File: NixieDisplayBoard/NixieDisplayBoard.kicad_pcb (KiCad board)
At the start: 2 copper layers, 43.2 x 53.3 mm, 4 parts, among them P1 CONN_01X12, P2 CONN_01X12

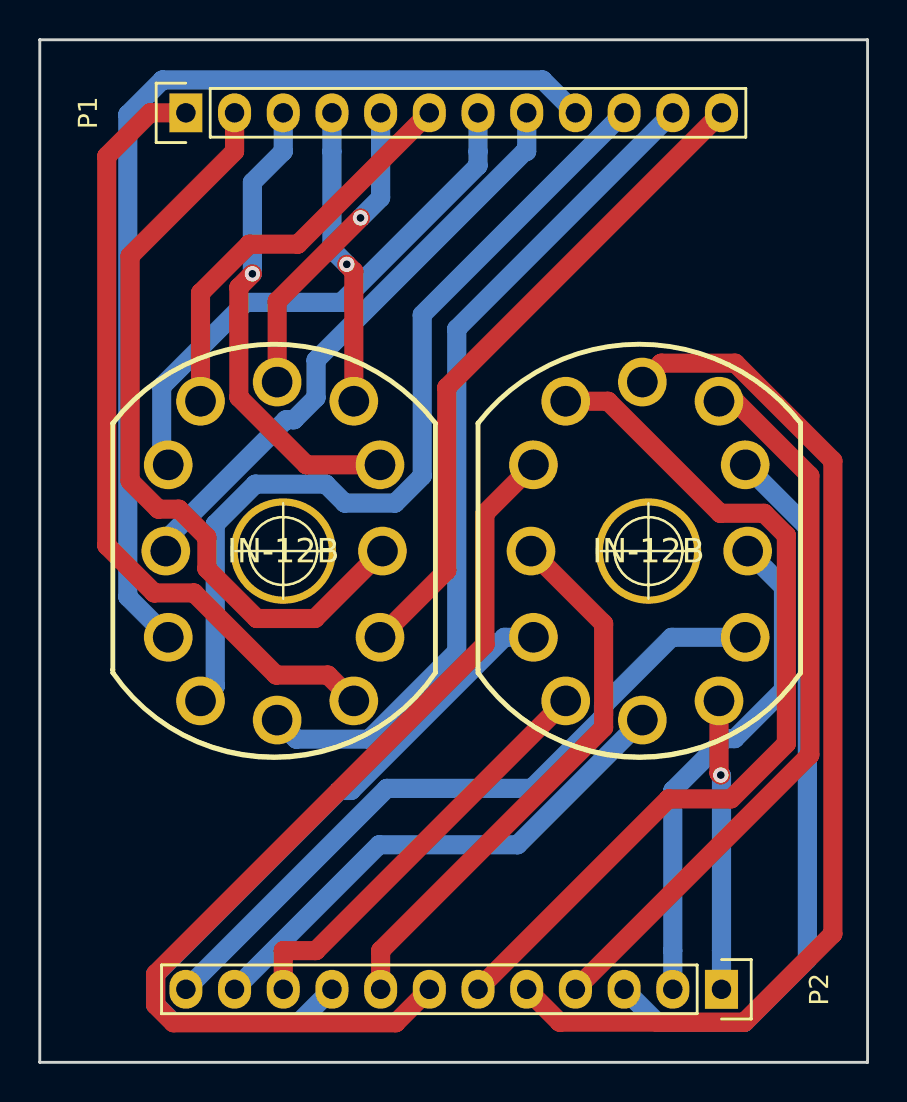
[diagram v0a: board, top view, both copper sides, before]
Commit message: Updates the display board to center the center-hole
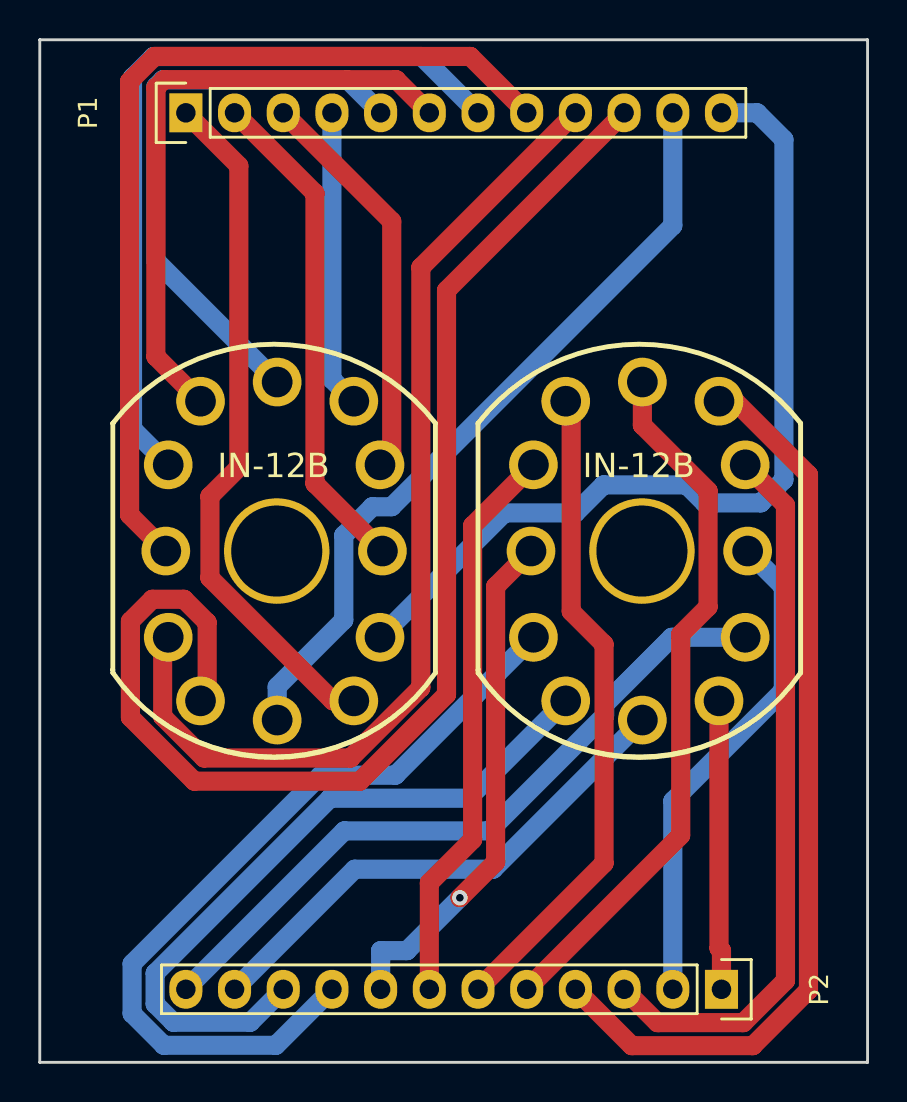
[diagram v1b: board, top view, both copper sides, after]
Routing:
- net Net-(N1-Pad1): track 45.5 -> 68.1 mm
- net Net-(N2-Pad4): track 51.7 -> 29.6 mm
- net Net-(N2-Pad6): track 55.7 -> 37.0 mm
- net Net-(N1-Pad3): track 31.0 -> 47.8 mm
- net Net-(N2-Pad1): track 22.1 -> 36.7 mm
- net Net-(N1-Pad6): track 16.3 -> 30.6 mm, vias 1 -> 0
- net Net-(N1-Pad9): track 40.0 -> 26.1 mm
- net Net-(N2-Pad5): track 46.7 -> 34.2 mm
- net Net-(N1-Pad4): track 28.3 -> 40.7 mm
- net Net-(N1-Pad0): track 34.7 -> 46.8 mm
- net Net-(N1-Pad5): track 21.5 -> 32.5 mm
- net Net-(N2-Pad7): track 38.2 -> 47.7 mm
- net Net-(N1-PadA): track 41.6 -> 36.2 mm
- net Net-(N2-Pad2): track 38.9 -> 42.9 mm
- net Net-(N1-Pad8): track 24.6 -> 21.0 mm, vias 1 -> 0
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
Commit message: Updates nixie boards
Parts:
- moved N1 1.27 mm to (124.5, 80.0)
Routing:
- net Net-(N1-Pad1): track 68.1 -> 110.4 mm
- net Net-(N2-Pad1): track 36.7 -> 22.5 mm, vias 0 -> 1
- net Net-(N2-Pad0): track 37.1 -> 50.6 mm
- net Net-(N2-Pad7): track 47.7 -> 35.8 mm
- net Net-(N1-Pad0): track 46.8 -> 35.2 mm
- net Net-(N1-Pad2): track 53.5 -> 42.1 mm
- net Net-(N2-Pad4): track 29.6 -> 36.3 mm
- net Net-(N2-Pad8): track 37.8 -> 32.8 mm
- net Net-(N1-PadLHDP): track 40.8 -> 45.7 mm, vias 0 -> 1
- net Net-(N2-Pad6): track 37.0 -> 41.1 mm
- net Net-(N2-Pad2): track 42.9 -> 39.3 mm
- net Net-(N1-PadA): track 36.2 -> 34.0 mm
- net Net-(N2-Pad9): track 26.0 -> 24.6 mm
- net Net-(N2-Pad5): track 34.2 -> 33.4 mm
- net Net-(N2-Pad3): track 26.9 -> 26.3 mm

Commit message: Makes the nixie breakout board less stupid about which pins mean what...
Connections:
- P1 pad 10: Net-(N1-Pad1) -> Net-(N1-Pad8)
- P1 pad 11: Net-(N1-PadLHDP) -> Net-(N1-Pad9)
- P1 pad 12: Net-(N1-Pad0) -> Net-(N1-PadLHDP)
- P1 pad 2: Net-(N1-Pad9) -> Net-(N1-Pad0)
- P1 pad 3: Net-(N1-Pad8) -> Net-(N1-Pad1)
- P1 pad 4: Net-(N1-Pad7) -> Net-(N1-Pad2)
- P1 pad 5: Net-(N1-Pad6) -> Net-(N1-Pad3)
- P1 pad 6: Net-(N1-Pad5) -> Net-(N1-Pad4)
- P1 pad 7: Net-(N1-Pad4) -> Net-(N1-Pad5)
- P1 pad 8: Net-(N1-Pad3) -> Net-(N1-Pad6)
- P1 pad 9: Net-(N1-Pad2) -> Net-(N1-Pad7)
- P2 pad 10: Net-(N2-Pad1) -> Net-(N2-Pad8)
- P2 pad 11: Net-(N2-PadLHDP) -> Net-(N2-Pad9)
- P2 pad 12: Net-(N2-Pad0) -> Net-(N2-PadLHDP)
- P2 pad 2: Net-(N2-Pad9) -> Net-(N2-Pad0)
- P2 pad 3: Net-(N2-Pad8) -> Net-(N2-Pad1)
- P2 pad 4: Net-(N2-Pad7) -> Net-(N2-Pad2)
- P2 pad 5: Net-(N2-Pad6) -> Net-(N2-Pad3)
- P2 pad 6: Net-(N2-Pad5) -> Net-(N2-Pad4)
- P2 pad 7: Net-(N2-Pad4) -> Net-(N2-Pad5)
- P2 pad 8: Net-(N2-Pad3) -> Net-(N2-Pad6)
- P2 pad 9: Net-(N2-Pad2) -> Net-(N2-Pad7)
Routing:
- net Net-(N1-Pad1): track 110.4 -> 38.6 mm
- net Net-(N2-Pad0): track 50.6 -> 20.6 mm
- net Net-(N2-Pad7): track 35.8 -> 58.2 mm
- net Net-(N2-Pad8): track 32.8 -> 52.8 mm
- net Net-(N2-Pad2): track 39.3 -> 19.3 mm
- net Net-(N2-Pad9): track 24.6 -> 43.5 mm
- net Net-(N1-Pad3): track 48.1 -> 29.4 mm
- net Net-(N1-Pad4): track 40.3 -> 25.0 mm
- net Net-(N1-Pad5): track 32.1 -> 21.6 mm
- net Net-(N1-Pad6): track 30.2 -> 20.9 mm
- net Net-(N1-Pad2): track 42.1 -> 33.9 mm
- net Net-(N2-Pad4): track 36.3 -> 28.7 mm
- net Net-(N2-Pad1): track 22.5 -> 16.1 mm, vias 1 -> 0
- net Net-(N1-PadA): track 34.0 -> 39.4 mm
- net Net-(N1-Pad0): track 35.2 -> 30.1 mm
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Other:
- board text added: "REV 3"

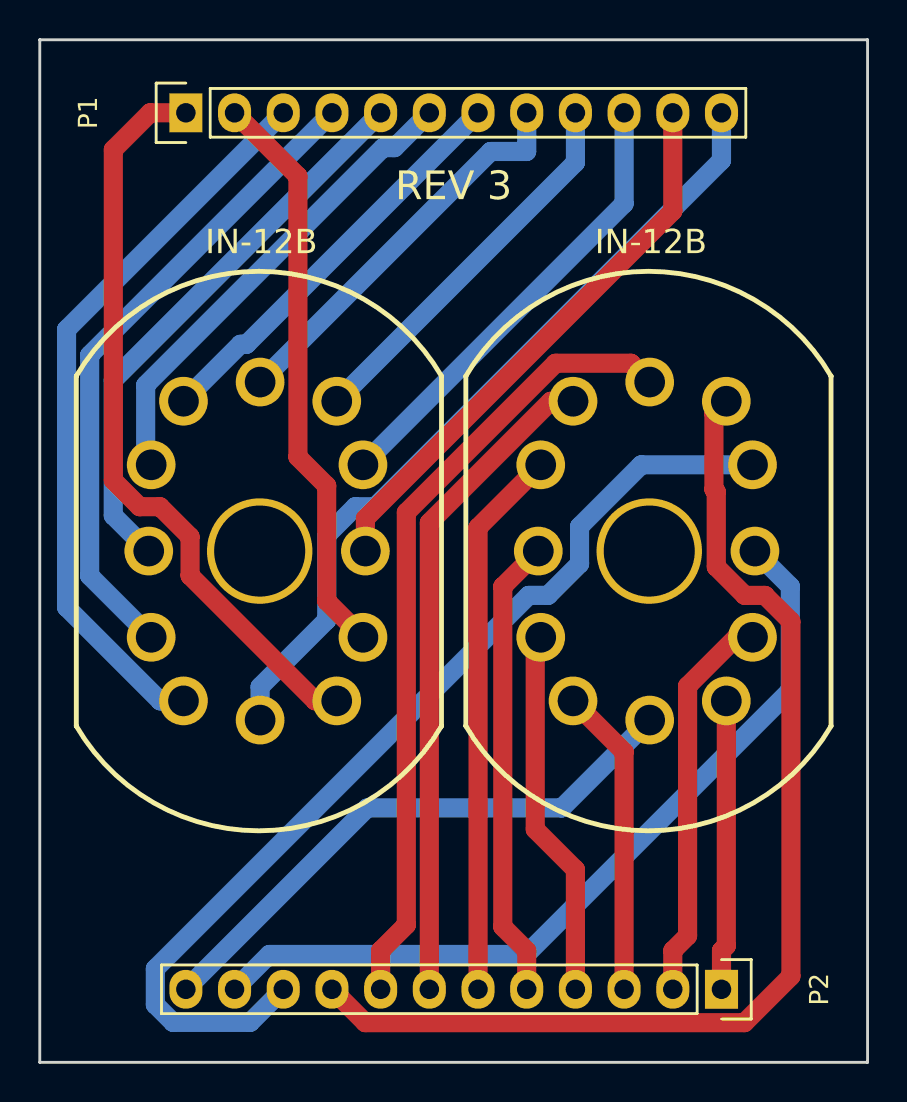
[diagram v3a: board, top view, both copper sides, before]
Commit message: Makes driver board more intuitive, and cleans up the silkscreen layers on both boards
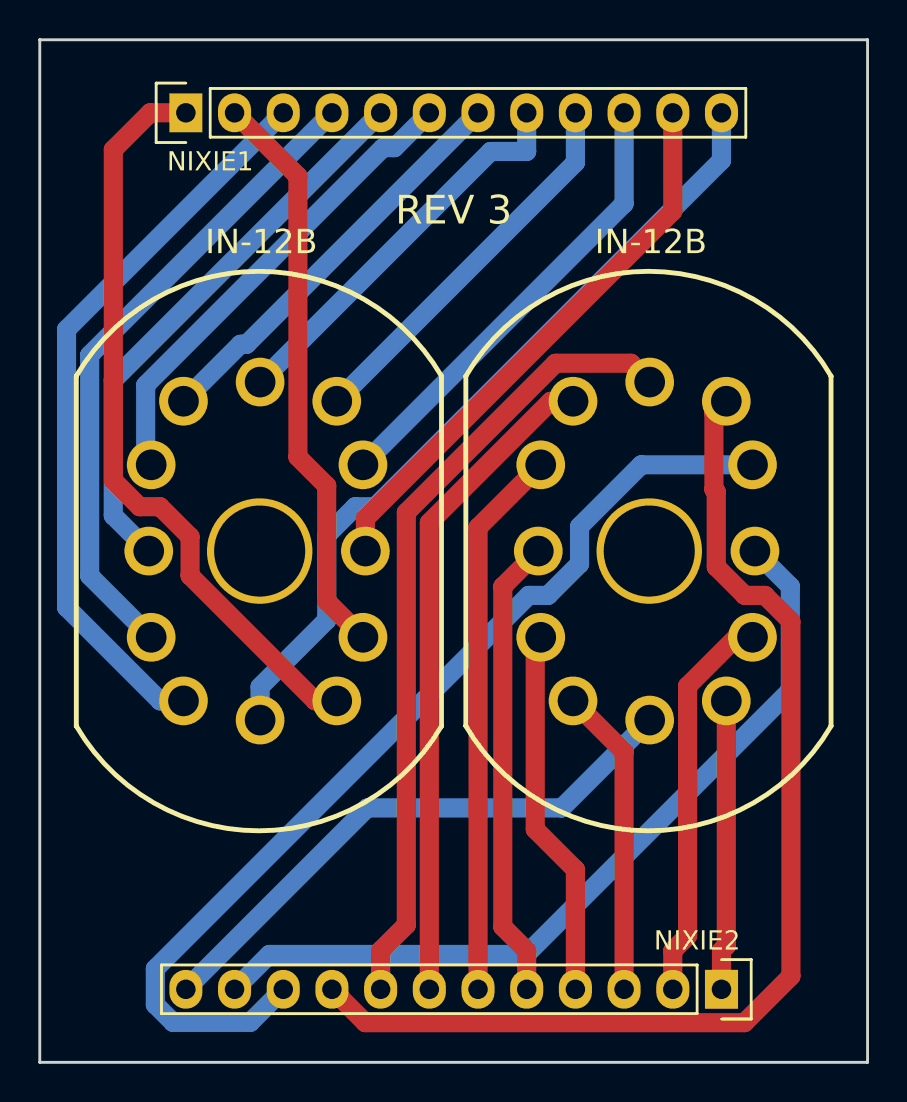
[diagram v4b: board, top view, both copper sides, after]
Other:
- board text added: "NIXIE1"
- board text added: "NIXIE2"
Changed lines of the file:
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@@
     (area 112.954999 53.264999 156.285001 106.755001)
     (thickness 1.6)
-    (drawings 5)
+    (drawings 7)
     (tracks 107)
     (zones 0)
@@
     (descr "Through hole pin header")
     (tags "pin header")
-    (fp_text reference P1 (at 0 -5.1 90) (layer F.SilkS)
+    (fp_text reference P1 (at 0 -5.1 90) (layer F.Fab)
       (effects (font (size 1 1) (thickness 0.15)))
     )
@@
     (descr "Through hole pin header")
     (tags "pin header")
-    (fp_text reference P2 (at 0 -5.1 270) (layer F.SilkS)
+    (fp_text reference P2 (at 0 -5.1 270) (layer F.Fab)
       (effects (font (size 1 1) (thickness 0.15)))
     )
@@
     (tags "MAY BE USED WITH SOCKET: SK-136")
     (attr virtual)
-    (fp_text reference N1 (at 10.69848 0.0635 90) (layer B.SilkS)
+    (fp_text reference N1 (at 10.69848 0.0635 90) (layer F.Fab)
       (effects (font (size 1.27 1.27) (thickness 0.0889)))
     )
@@
     (tags "MAY BE USED WITH SOCKET: SK-136")
     (attr virtual)
-    (fp_text reference N2 (at 10.69848 0.0635 90) (layer B.SilkS)
+    (fp_text reference N2 (at 10.69848 0.0635 90) (layer F.Fab)
       (effects (font (size 1.27 1.27) (thickness 0.0889)))
     )
@@
     (pad "" thru_hole circle (at 0.041 0) (size 5.5 5.5) (drill 4.75) (layers *.Cu))
   )
-  (gr_text "REV 3" (at 134.62 60.96) (layer F.SilkS)
+  (gr_text NIXIE2 (at 147.32 100.33) (layer F.SilkS)
+    (effects (font (size 1 1) (thickness 0.15)))
+  )
+  (gr_text NIXIE1 (at 121.92 59.69) (layer F.SilkS)
+    (effects (font (size 1 1) (thickness 0.15)))
+  )
+  (gr_text "REV 3" (at 134.62 62.23) (layer F.SilkS)
     (effects (font (size 1.5 1.5) (thickness 0.3)))
   )
